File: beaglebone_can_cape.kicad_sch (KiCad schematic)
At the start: 20 parts, among them J1 DCAN0, J2 DCAN1, P8 BeagleBone_Black_Header, P9 BeagleBone_Black_Header, U1 TCAN332, U2 TCAN332, U3 LMR51430

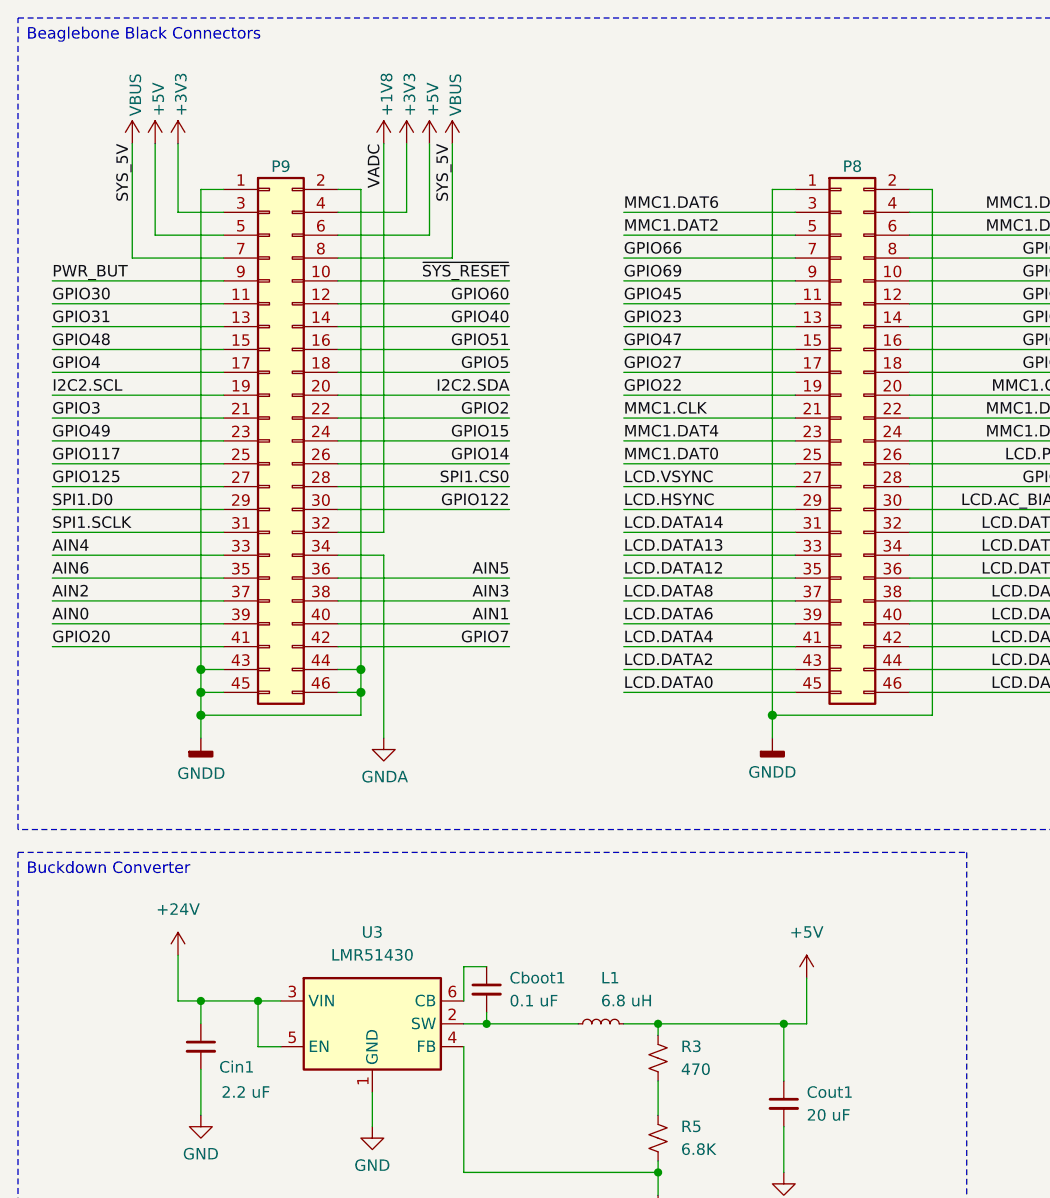
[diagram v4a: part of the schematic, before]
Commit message: Symbol may not be needed, we will see...
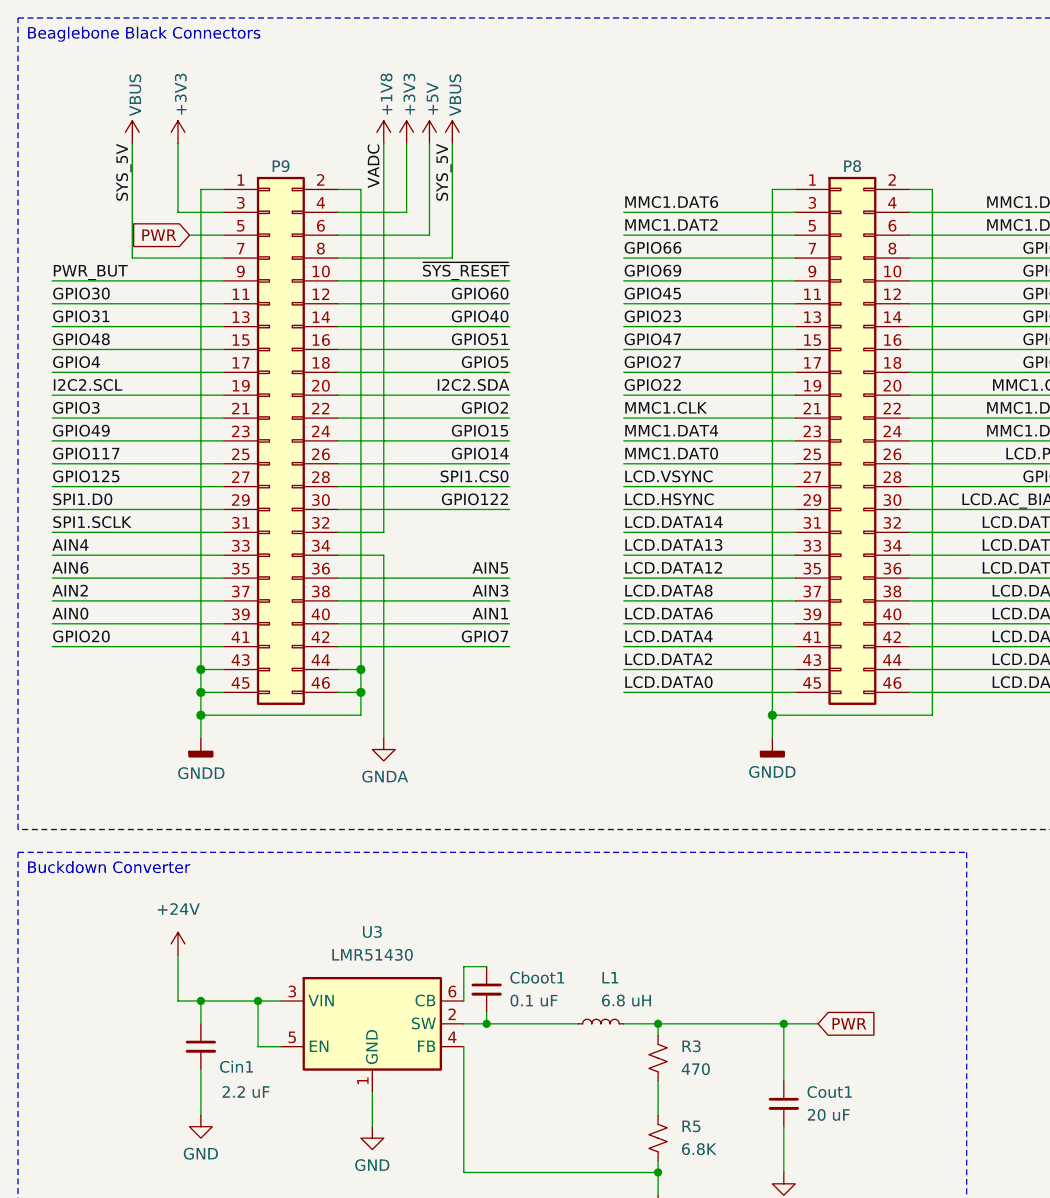
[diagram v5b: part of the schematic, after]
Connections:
- net +5V: no longer Cout1.1, L1.2, P9.5 (Pin_5), R3.1
- new net PWR: Cout1.1, L1.2, P9.5 (Pin_5), R3.1
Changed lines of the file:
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@@
 	(wire
 		(pts
-			(xy 38.1 39.37) (xy 30.48 39.37)
-		)
-		(stroke
-			(width 0)
-			(type solid)
-		)
-	)
-	(wire
-		(pts
 			(xy 55.88 74.93) (xy 55.88 95.25)
 		)
@@
 	(wire
 		(pts
-			(xy 30.48 39.37) (xy 30.48 29.21)
-		)
-		(stroke
-			(width 0)
-			(type solid)
-		)
-	)
-	(wire
-		(pts
 			(xy 82.55 49.53) (xy 101.6 49.53)
 		)
@@
 	(wire
 		(pts
+			(xy 34.29 39.37) (xy 38.1 39.37)
+		)
+		(stroke
+			(width 0)
+			(type solid)
+		)
+	)
+	(wire
+		(pts
 			(xy 82.55 87.63) (xy 101.6 87.63)
 		)
@@
 	(wire
 		(pts
-			(xy 102.87 121.92) (xy 102.87 127)
-		)
-		(stroke
-			(width 0)
-			(type default)
-		)
-	)
-	(wire
-		(pts
 			(xy 185.42 33.02) (xy 185.42 34.29)
 		)
@@
 	(wire
 		(pts
-			(xy 102.87 127) (xy 100.33 127)
+			(xy 100.33 127) (xy 104.14 127)
 		)
 		(stroke
@@
 		)
 	)
+	(global_label "PWR"
+		(shape input)
+		(at 104.14 127 0)
+		(fields_autoplaced yes)
+		(effects
+			(font
+				(size 1.27 1.27)
+			)
+			(justify left)
+		)
+		(property "Intersheetrefs" "${INTERSHEET_REFS}"
+			(at 111.2117 127 0)
+			(effects
+				(font
+					(size 1.27 1.27)
+				)
+				(justify left)
+				(hide yes)
+			)
+		)
+	)
+	(global_label "PWR"
+		(shape input)
+		(at 34.29 39.37 180)
+		(fields_autoplaced yes)
+		(effects
+			(font
+				(size 1.27 1.27)
+			)
+			(justify right)
+		)
+		(property "Intersheetrefs" "${INTERSHEET_REFS}"
+			(at 27.2183 39.37 0)
+			(effects
+				(font
+					(size 1.27 1.27)
+				)
+				(justify right)
+				(hide yes)
+			)
+		)
+	)
 	(symbol
 		(lib_id "power:GNDD")
@@
 	)
 	(symbol
-		(lib_id "power:+5V")
-		(at 30.48 29.21 0)
-		(unit 1)
-		(exclude_from_sim no)
-		(in_bom yes)
-		(on_board yes)
-		(dnp no)
-		(property "Reference" "#PWR09"
-			(at 30.48 33.02 0)
-			(effects
-				(font
-					(size 1.27 1.27)
-				)
-				(hide yes)
-			)
-		)
-		(property "Value" "+5V"
-			(at 30.861 26.162 90)
-			(effects
-				(font
-					(size 1.27 1.27)
-				)
-				(justify left)
-			)
-		)
-		(property "Footprint" ""
-			(at 30.48 29.21 0)
-			(effects
-				(font
-					(size 1.524 1.524)
-				)
-			)
-		)
-		(property "Datasheet" ""
-			(at 30.48 29.21 0)
-			(effects
-				(font
-					(size 1.524 1.524)
-				)
-			)
-		)
-		(property "Description" "Power symbol creates a global label with name \"+5V\""
-			(at 30.48 29.21 0)
-			(effects
-				(font
-					(size 1.27 1.27)
-				)
-				(hide yes)
-			)
-		)
-		(pin "1"
-		)
-		(instances
-			(project "BeagleBone-Black-Cape"
-				(path "/e63e39d7-6ac0-4ffd-8aa3-1841a4541b55"
-					(reference "#PWR09")
-					(unit 1)
-				)
-			)
-		)
-	)
-	(symbol
 		(lib_id "Connector_Generic:Conn_02x23_Odd_Even")
 		(at 43.18 62.23 0)
@@
 					(unit 1)
 				)
-			)
-		)
-	)
-	(symbol
-		(lib_id "power:+5V")
-		(at 102.87 121.92 0)
-		(unit 1)
-		(exclude_from_sim no)
-		(in_bom yes)
-		(on_board yes)
-		(dnp no)
-		(fields_autoplaced yes)
-		(property "Reference" "#PWR016"
-			(at 102.87 125.73 0)
-			(effects
-				(font
-					(size 1.27 1.27)
-				)
-				(hide yes)
-			)
-		)
-		(property "Value" "+5V"
-			(at 102.87 116.84 0)
-			(effects
-				(font
-					(size 1.27 1.27)
-				)
-			)
-		)
-		(property "Footprint" ""
-			(at 102.87 121.92 0)
-			(effects
-				(font
-					(size 1.27 1.27)
-				)
-				(hide yes)
-			)
-		)
-		(property "Datasheet" ""
-			(at 102.87 121.92 0)
-			(effects
-				(font
-					(size 1.27 1.27)
-				)
-				(hide yes)
-			)
-		)
-		(property "Description" "Power symbol creates a global label with name \"+5V\""
-			(at 102.87 121.92 0)
-			(effects
-				(font
-					(size 1.27 1.27)
-				)
-				(hide yes)
-			)
-		)
-		(pin "1"
-		)
-		(instances
-			(project ""
-				(path "/e63e39d7-6ac0-4ffd-8aa3-1841a4541b55"
-					(reference "#PWR016")
-					(unit 1)
-				)

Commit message: pushing schem from added deutsch
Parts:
- added J3: DTM15-12PA, DTM15-12PA:TE_DTM15-12PA, symbol Senior_Design:DTM15-12PA
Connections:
- net GND: now also J3.12
- net CAN HIGH 1: now reaches J2.2 (Pin_2), JP2.1 (A), U2.7 (CANH)
- net CAN HIGH 1: now also J3.10, J3.9
- net CAN LOW 1: now reaches J2.1 (Pin_1), R2.2, U2.6 (CANL)
- net CAN LOW 1: now also J3.7, J3.8
- new net BAT: J3.1
- new net CAN HIGH 0: J3.2, J3.3
- new net CAN LOW 0: J3.4, J3.5
- new net CAN SHLD 0: J3.6
- new net CAN SHLD 1: J3.11

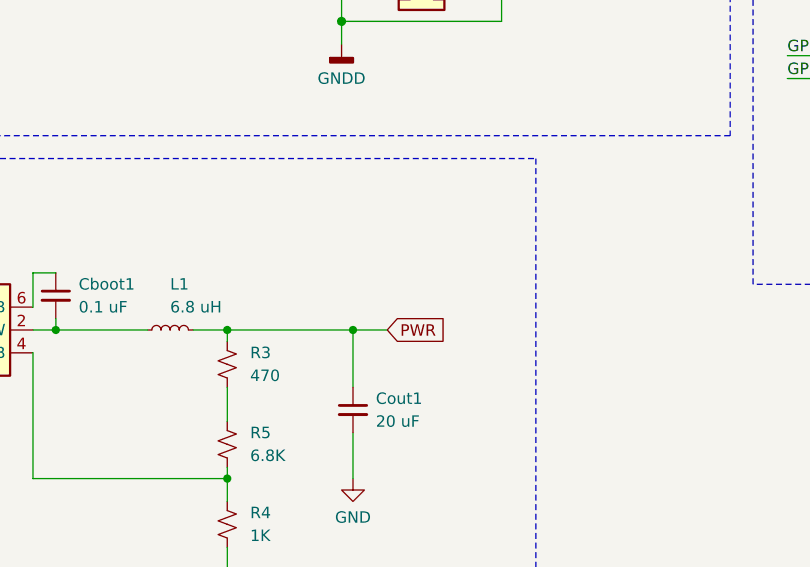
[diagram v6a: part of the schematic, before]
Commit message: Schematic + PCB support of Deutsch
* Imported the DTM15-12PA footprint (this one is not correct as Marlin has a smaller footprint I know now)
* Removed "PWR" label and replaced with 5V net
* Reviewed the new schematic fooprint that Zach added, looks good
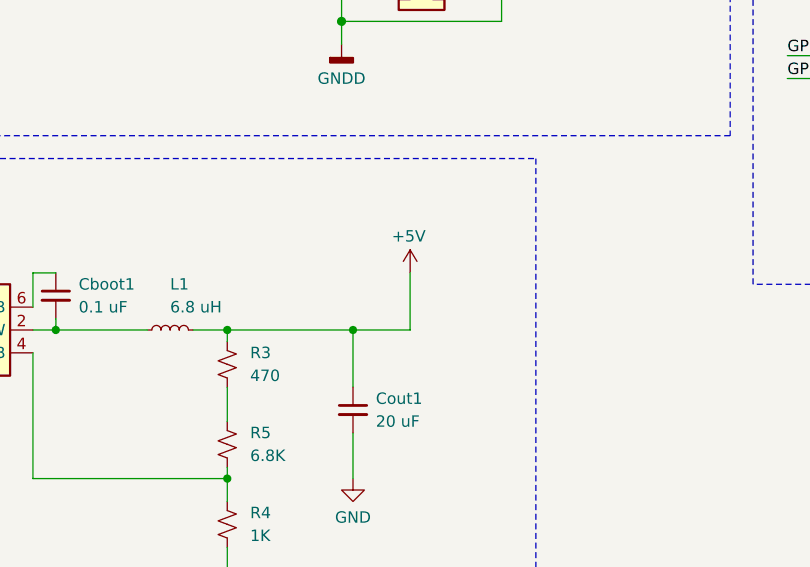
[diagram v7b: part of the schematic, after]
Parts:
- J3: footprint DTM15-12PA:TE_DTM15-12PA -> Senior Design:TE_DTM15-12PA
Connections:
- net +5V: now also Cout1.1, L1.2, R3.1
- net PWR: no longer Cout1.1, L1.2, R3.1
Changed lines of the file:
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@@
 	(wire
 		(pts
+			(xy 106.68 120.65) (xy 106.68 127)
+		)
+		(stroke
+			(width 0)
+			(type default)
+		)
+	)
+	(wire
+		(pts
 			(xy 196.85 140.97) (xy 203.2 140.97)
 		)
@@
 	(wire
 		(pts
-			(xy 100.33 127) (xy 104.14 127)
+			(xy 100.33 127) (xy 106.68 127)
 		)
 		(stroke
@@
 		)
 	)
-	(global_label "PWR"
-		(shape input)
-		(at 104.14 127 0)
-		(fields_autoplaced yes)
-		(effects
-			(font
-				(size 1.27 1.27)
-			)
-			(justify left)
-		)
-		(property "Intersheetrefs" "${INTERSHEET_REFS}"
-			(at 111.2117 127 0)
-			(effects
-				(font
-					(size 1.27 1.27)
-				)
-				(justify left)
-				(hide yes)
-			)
-		)
-	)
 	(global_label "CAN SHLD 0"
 		(shape input)
@@
 			)
 		)
-		(property "Footprint" "DTM15-12PA:TE_DTM15-12PA"
+		(property "Footprint" "Senior Design:TE_DTM15-12PA"
 			(at 213.36 143.51 0)
 			(effects
@@
 					(unit 1)
 				)
+			)
+		)
+	)
+	(symbol
+		(lib_id "power:+5V")
+		(at 106.68 120.65 0)
+		(unit 1)
+		(exclude_from_sim no)
+		(in_bom yes)
+		(on_board yes)
+		(dnp no)
+		(property "Reference" "#PWR016"
+			(at 106.68 124.46 0)
+			(effects
+				(font
+					(size 1.27 1.27)
+				)
+				(hide yes)
+			)
+		)
+		(property "Value" "+5V"
+			(at 104.648 116.586 0)
+			(effects
+				(font
+					(size 1.27 1.27)
+				)
+				(justify left)
+			)
+		)
+		(property "Footprint" ""
+			(at 106.68 120.65 0)
+			(effects
+				(font
+					(size 1.524 1.524)
+				)
+			)
+		)
+		(property "Datasheet" ""
+			(at 106.68 120.65 0)
+			(effects
+				(font
+					(size 1.524 1.524)
+				)
+			)
+		)
+		(property "Description" "Power symbol creates a global label with name \"+5V\""
+			(at 106.68 120.65 0)
+			(effects
+				(font
+					(size 1.27 1.27)
+				)
+				(hide yes)
+			)
+		)
+		(pin "1"
+		)
+		(instances
+			(project "beaglebone_can_cape"
+				(path "/e63e39d7-6ac0-4ffd-8aa3-1841a4541b55"
+					(reference "#PWR016")
+					(unit 1)
+				)

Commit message: taking break, letting Nash cook
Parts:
- added J4: Conn_02x02_Top_Bottom, Connector_PinHeader_2.54mm:PinHeader_2x02_P2.54mm_Vertical, symbol Connector_Generic:Conn_02x02_Top_Bottom
- added J5: Battery Harness, SeniorDesign:BatteryHolder, symbol Senior_Design:BatteryHolder
- added JP3: Jumper_2_Open, symbol Jumper:Jumper_2_Open
- added R6: 10k, Resistor_SMD:R_0805_2012Metric, symbol Device:R_Small_US
- J3: footprint Senior Design:TE_DTM15-12PA -> DTM15-12PA:TE_DTM15-12PA
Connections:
- net +5V: no longer Cout1.1, L1.2, R3.1
- net PWR: now also Cout1.1, L1.2, R3.1
- new net: J4.1 (Pin_1), J4.2 (Pin_2), J5.1 (Vout)
- new net: J4.3 (Pin_3), JP3.1 (A)
- new net: J4.4 (Pin_4), J5.2 (Gnd), R6.2
- new net: JP3.2 (B), R6.1
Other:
- moved on the sheet: Cboot1, Cin1, Cout1, L1, R3, R4, R5, U3
